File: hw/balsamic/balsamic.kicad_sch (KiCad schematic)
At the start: 50 parts, among them J1 Conn_01x24, J3 USB_B_Mini, SW1 SW_Push, U1 ISP1807-LR-RS, U2 BMI160, U4 MAX77658AANX+

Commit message: switched to mezzanine camera connector
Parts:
- removed AE?: Antenna_Chip, symbol Device:Antenna_Chip
- removed J1: Conn_01x24, Connector_FFC-FPC:Hirose_FH12-24S-0.5SH_1x24-1MP_P0.50mm_Horizontal, symbol Connector_Generic:Conn_01x24
- removed R1, R2, R3: 0, Resistor_SMD:R_0402_1005Metric, symbol Device:R_Small
- removed R17, R18: 0, Resistor_SMD:R_0201_0603Metric, symbol Device:R_Small
- added J2: AXT524124, footprints:PANASONIC_AXT524124, symbol AXT524124-mezzanine-conn:AXT524124
- J3: footprint Connector_USB:USB_Micro-B_Amphenol_10118194_Horizontal -> Connector_USB:USB_Micro-B_GCT_USB3076-30-A
- TP14, TP15, TP16, TP17, TP18, TP19, TP20, TP5: footprint TestPoint:TestPoint_Pad_D1.0mm -> custom_testpoints:TestPoint_Pad_D0.5mm
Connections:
- net +1V8: now also J2.10, J2.11
- net +3V0: now also J2.4
- net +3V3: now also J2.24
- net DVP_D0: now also J2.19
- net DVP_D1: now also J2.21
- net DVP_D2: now also J2.22
- net DVP_D3: now also J2.20
- net DVP_D4: now also J2.18
- net DVP_D5: now also J2.16
- net DVP_D6: now also J2.14
- net DVP_D7: now also J2.12
- net DVP_HSYNC: now also J2.9
- net DVP_PCLK: now also J2.17
- net DVP_PWDN: now also J2.8
- net DVP_RST: now also J2.6
- net DVP_SCL: now also J2.5
- net DVP_SDA: now also J2.3
- net DVP_VSYNC: now also J2.7
- net DVP_XCLK: now also J2.13
- net GND: now also U1.20 (OUT_ANT), U1.22 (OUT_MOD), J2.15, J2.23, J2.S1 (SHIELD), J2.S2 (SHIELD), J2.S3 (SHIELD), J2.S4 (SHIELD)
- net GNDA: now also J2.2
- net nRF_SWDCLK: now also J3.2 (D-)
- net nRF_SWDIO: now also J3.3 (D+)
- no-connect marks 51 -> 52
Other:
- note added: "Need to double check this pin assignment for new connector."
- moved on the sheet: C47, C48, C49, C50, R15, R16

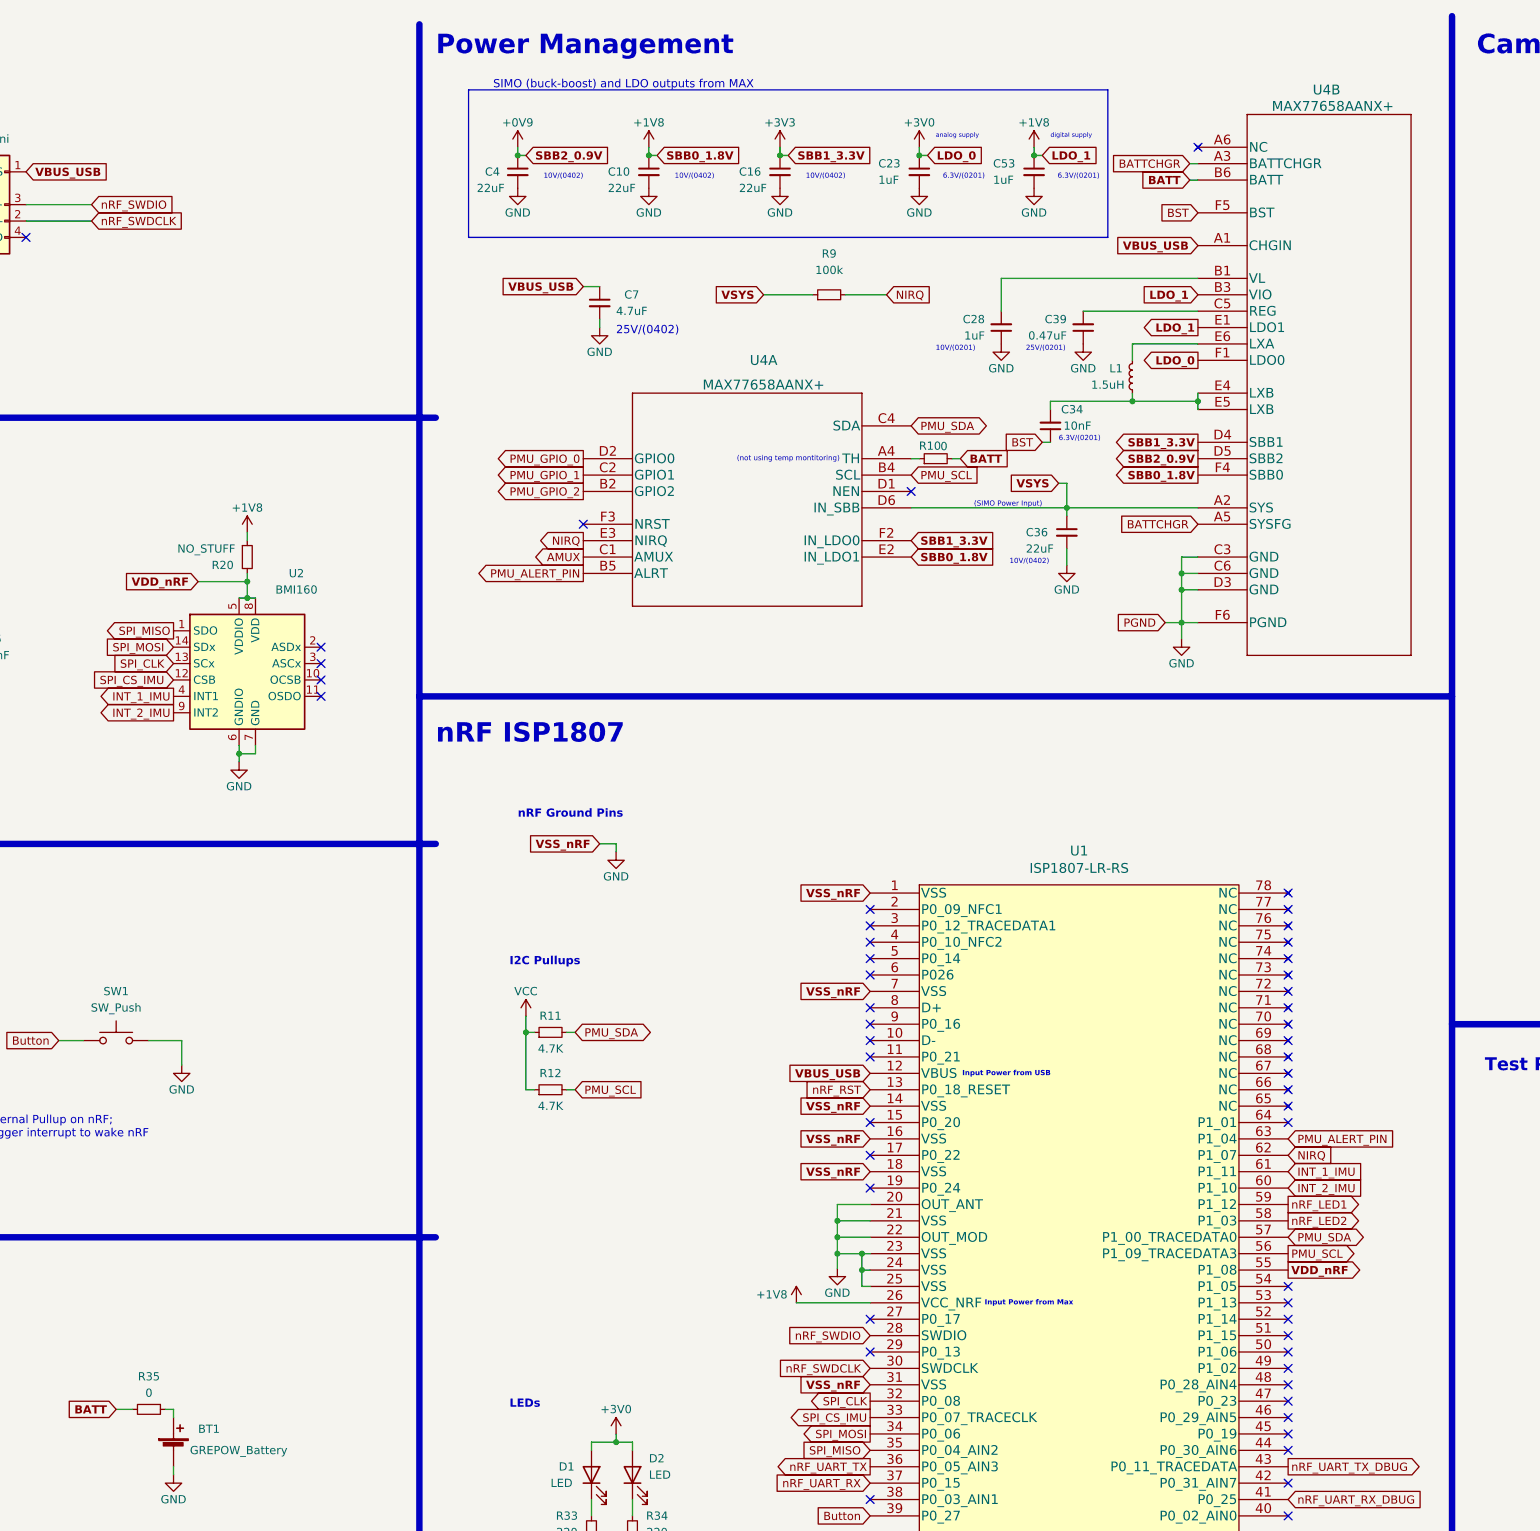
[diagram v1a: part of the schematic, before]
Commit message: changed PMU to MAX77651
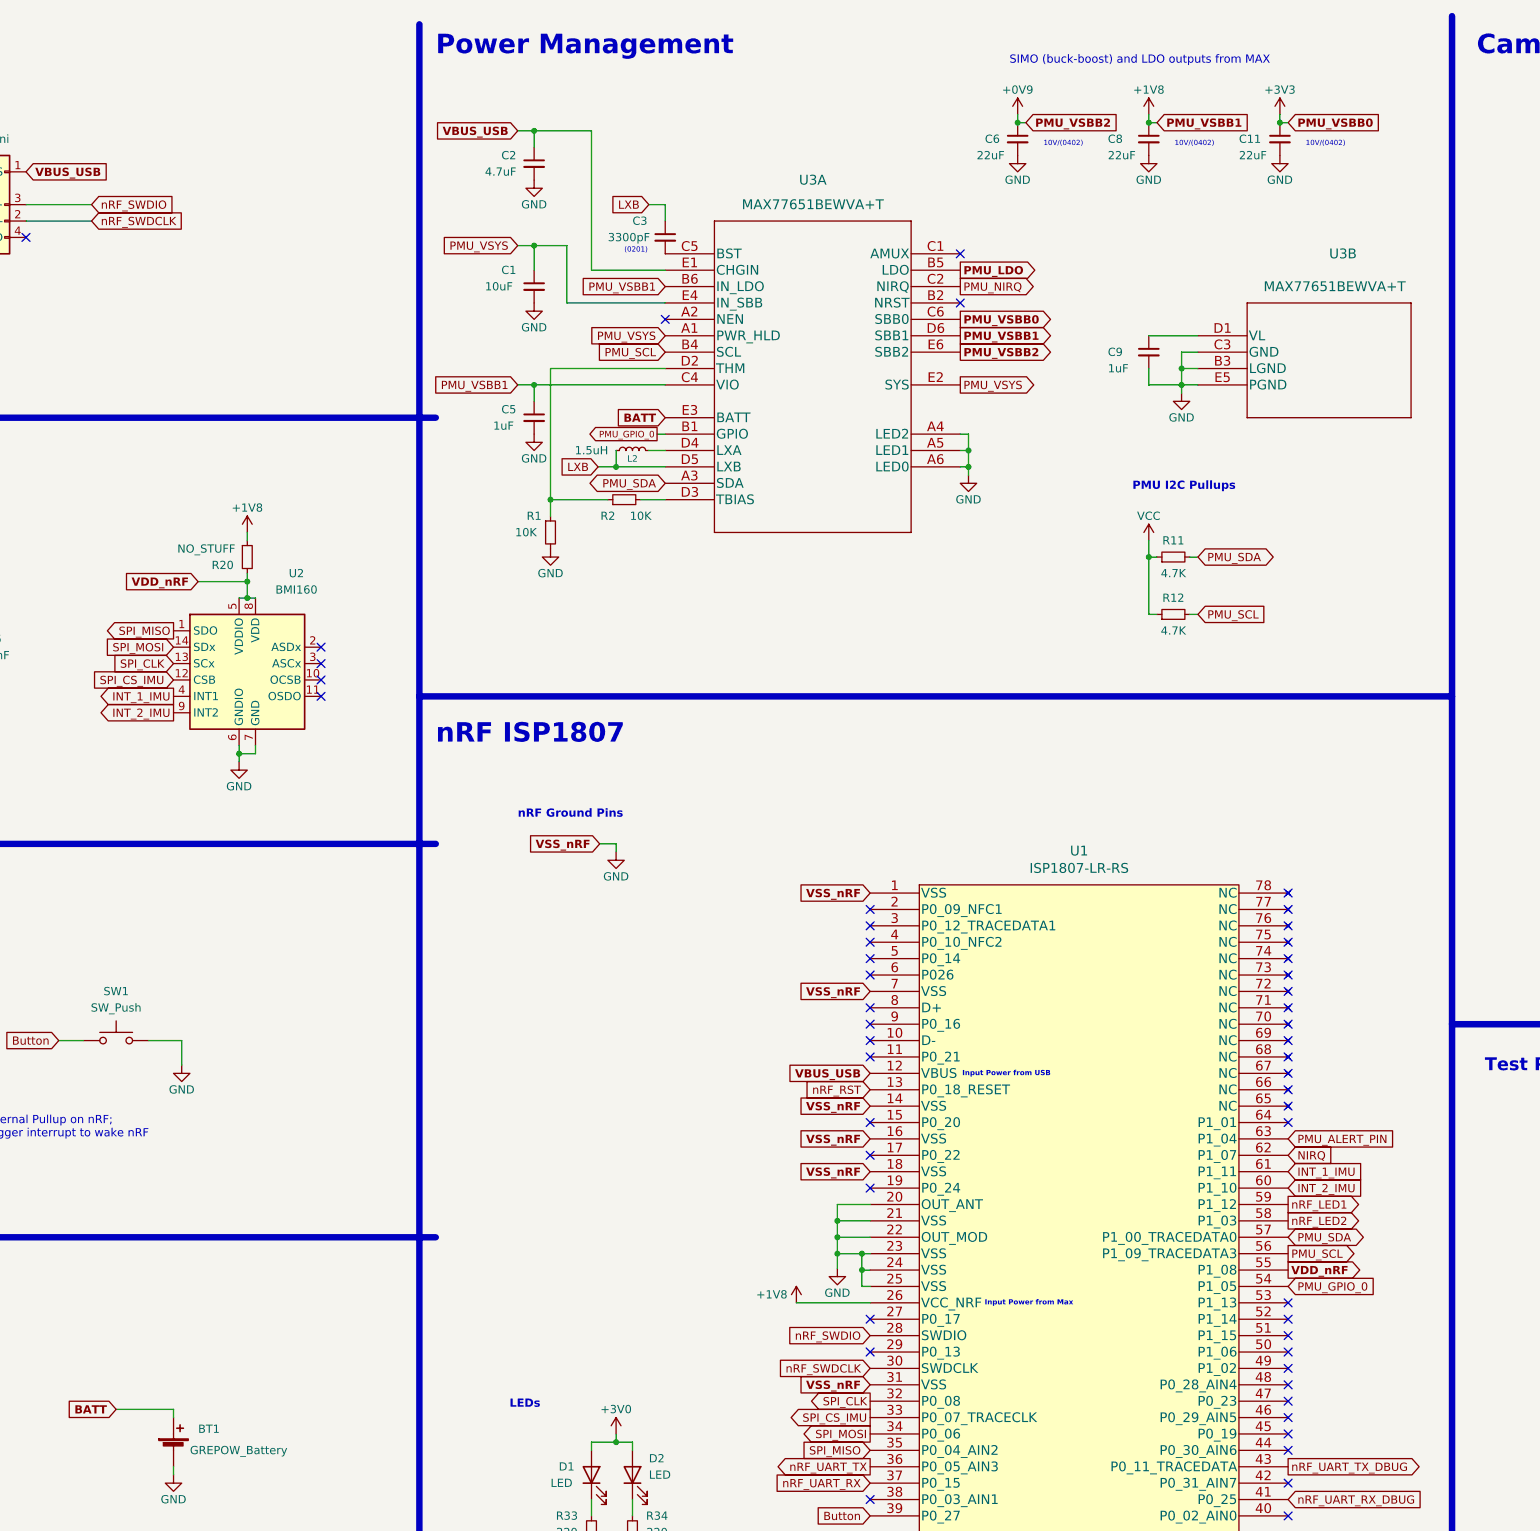
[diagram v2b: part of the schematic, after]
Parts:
- removed C10, C16, C36, C4: 22uF, Capacitor_SMD:C_0201_0603Metric, symbol Device:C_Small
- removed C23, C28, C53: 1uF, Capacitor_SMD:C_0201_0603Metric, symbol Device:C_Small
- removed C34: 10nF, Capacitor_SMD:C_0201_0603Metric, symbol Device:C_Small
- removed C39: 0.47uF, Capacitor_SMD:C_0201_0603Metric, symbol Device:C_Small
- removed C7: 4.7uF, Capacitor_SMD:C_0201_0603Metric, symbol Device:C_Small
- removed L1: 1.5uH, Inductor_SMD:L_0805_2012Metric, symbol Device:L_Small
- removed R10: 0, Resistor_SMD:R_0201_0603Metric, symbol Device:R_Small
- removed R35: 0, Resistor_SMD:R_0402_1005Metric, symbol Device:R_Small
- removed R9: 100k, Resistor_SMD:R_0201_0603Metric, symbol Device:R_Small
- removed U4: MAX77658AANX+, footprints:MAX77658AANX&plus_, symbol max77658_functional:MAX77658AANX+
- added C1: 10uF, Capacitor_SMD:C_0201_0603Metric, symbol Device:C_Small
- added C11, C6, C8: 22uF, Capacitor_SMD:C_0201_0603Metric, symbol Device:C_Small
- added C2: 4.7uF, Capacitor_SMD:C_0201_0603Metric, symbol Device:C_Small
- added C3: 3300pF, Capacitor_SMD:C_0201_0603Metric, symbol Device:C_Small
- added C5, C9: 1uF, Capacitor_SMD:C_0201_0603Metric, symbol Device:C_Small
- added L2: 1.5uH, Inductor_SMD:L_0805_2012Metric, symbol Device:L_Small
- added R1, R2: 10K, Resistor_SMD:R_0201_0603Metric, symbol Device:R_Small
- added U3: MAX77651BEWVA+T, footprints:MAX77651BEWVA&plus_T, symbol MAX77651BEWVA-T:MAX77651BEWVA+T
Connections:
- net +0V9: now also C6.1, U3.E6 (SBB2)
- net +1V8: now also C5.1, C8.1, U3.B6 (IN_LDO), U3.C4 (VIO), U3.D6 (SBB1)
- net +3V3: now also C11.1, U3.C6 (SBB0)
- net BATT: now also BT1.1 (+), U3.E3 (BATT)
- net GND: now also C1.2, C11.2, C2.2, C5.2, C6.2, C8.2, C9.2, R1.2, U3.A4 (LED2), U3.A5 (LED1), U3.A6 (LED0), U3.B3 (LGND), U3.C3 (GND), U3.E5 (PGND)
- net PMU_GPIO_0: now also U1.54 (P1_05), U3.B1 (GPIO)
- net PMU_SCL: now also U3.B4 (SCL)
- net PMU_SDA: now also U3.A3 (SDA)
- net VBUS_USB: now also C2.1, U3.E1 (CHGIN)
- new net: R1.1, R2.1, U3.D2 (THM)
- new net: R2.2, U3.D3 (TBIAS)
- new net: L2.2, U3.D4 (LXA)
- new net: C9.1, U3.D1 (VL)
- new net: C3.2, U3.C5 (BST)
- new net LXB: C3.1, L2.1, U3.D5 (LXB)
- new net PMU_LDO: U3.B5 (LDO)
- new net PMU_NIRQ: U3.C2 (NIRQ)
- new net PMU_VSYS: C1.1, U3.A1 (PWR_HLD), U3.E2 (SYS), U3.E4 (IN_SBB)
- no-connect marks 52 -> 51
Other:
- note added: "(0201)"
- note added: "PMU I2C Pullups"
- note removed: "(SIMO Power Input)"
- note removed: "(not using temp montitoring)"
- note removed: "10V/(0201)"
- note removed: "25V/(0201)"
- note removed: "25V/(0402)"
- note removed: "6.3V/(0201)"
- note removed: "I2C Pullups"
- note removed: "analog supply"
- note removed: "digital supply"
- moved on the sheet: R11, R12

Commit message: Got board size to 16.1x9.825mm
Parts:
- removed C46: 100nF, Capacitor_SMD:C_0402_1005Metric, symbol Device:C_Small
- removed J2: AXT524124, footprints:PANASONIC_AXT524124, symbol AXT524124-mezzanine-conn:AXT524124
- removed R11, R12: 4.7K, Resistor_SMD:R_0201_0603Metric, symbol Device:R_Small
- added C10: 10uF, Capacitor_SMD:C_0201_0603Metric, symbol Device:C_Small
- added C12: 100nf, Capacitor_SMD:C_0201_0603Metric, symbol Device:C_Small
- added C4: 4.7uF, Capacitor_SMD:C_0201_0603Metric, symbol Device:C_Small
- added C7: 22uF, Capacitor_SMD:C_0201_0603Metric, symbol Device:C_Small
- added J1: AXT524124, footprints:PANASONIC_AXT524124, symbol AXT524124-mezzanine-conn:AXT524124
- added TP1, TP10, TP11, TP12, TP13, TP2, TP3, TP4, TP6, TP7, TP8, TP9: TestPoint, custom_testpoints:TestPoint_Pad_D0.5mm, symbol Connector:TestPoint
- C1: value 10uF -> 22uF
- C11, C47, C6, C8: value 22uF -> 10uF
- C48: value 10uF -> 100nF
- L2: footprint Inductor_SMD:L_0805_2012Metric -> Inductor_SMD:L_0603_1608Metric
- R33, R34: value 220 -> 200
- SW1: footprint Button_Switch_SMD:SW_SPST_B3U-1000P -> Resistor_SMD:R_0603_1608Metric
- TP17, TP18, TP19, TP20: footprint custom_testpoints:TestPoint_Pad_D0.5mm -> custom_testpoints:TestPoint_THTPad_1.0x1.0mm_Drill0.5mm
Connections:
- net PMU_LDO is gone; now on net VDDA: U3.B5 (LDO)
- net PMU_SCL is gone; now on net DVP_SCL: U1.56 (P1_09_TRACEDATA3), U3.B4 (SCL)
- net +1V8: now also C6.1, D1.2 (A), D2.2 (A), SW1.2, TP17.1, C12.2, J1.3; no longer C49.1, C50.2
- net BATT: now also C4.1
- net Button: now also TP18.1, U1.33 (P0_07_TRACECLK); no longer U1.39 (P0_27)
- net DVP_D0: now also U1.15 (P0_20), J1.10, TP8.1
- net DVP_D1: now also TP16.1, U1.11 (P0_21), J1.12
- net DVP_D2: now also TP15.1, U1.17 (P0_22), J1.14
- net DVP_D3: now also U1.47 (P0_23), J1.16, TP2.1
- net DVP_D4: now also J1.18
- net DVP_D5: now also J1.20
- net DVP_D6: now also J1.22
- net DVP_D7: now also J1.24
- net DVP_PCLK: now also U1.45 (P0_19), J1.8, TP9.1
- net DVP_SCL: now also J1.11
- net DVP_SDA: now also U1.3 (P0_12_TRACEDATA1), J1.9
- net GND: now also C10.2, C12.1, C4.2, C7.2, J1.19, J1.2, J1.5, J1.6, J1.S1 (SHIELD), J1.S2 (SHIELD), J1.S3 (SHIELD), J1.S4 (SHIELD); no longer SW1.2
- net GNDA: now also J1.23
- net PMU_NIRQ: now also U1.62 (P1_07)
- net PMU_VSYS: now also C7.1
- net nRF_LED1: now also TP19.1, U1.32 (P0_08); no longer U1.59 (P1_12)
- net nRF_LED2: now also TP20.1, U1.34 (P0_06); no longer U1.58 (P1_03)
- net nRF_UART_TX: now also TP7.1
- net IMU_MISO: now reaches U1.19 (P0_24)
- net IMU_MISO: now also U2.1 (SDO), TP3.1
- net DVP_INT: now reaches U1.2 (P0_09_NFC1)
- net DVP_INT: now also J1.7, TP11.1
- net IMU_CLK: now reaches U1.27 (P0_17)
- net IMU_CLK: now also TP5.1, U2.13 (SCx)
- net IMU_CS: now reaches U1.29 (P0_13)
- net IMU_CS: now also U2.12 (CSB), TP6.1
- net nRF_P0_03: now reaches U1.38 (P0_03_AIN1)
- net nRF_P0_02: now reaches U1.40 (P0_02_AIN0)
- net nRF_P0_31: now reaches U1.42 (P0_31_AIN7)
- net nRF_P0_30: now reaches U1.44 (P0_30_AIN6)
- net DVP_FVLD: now reaches U1.46 (P0_29_AIN5)
- net DVP_FVLD: now also J1.15, TP13.1
- net DVP_LVLD: now reaches U1.48 (P0_28_AIN4)
- net DVP_LVLD: now also J1.13, TP12.1
- net IMU_INT2: now reaches U1.49 (P1_02)
- net IMU_INT2: now also U2.9 (INT2)
- net nRF_P1_06: now reaches U1.50 (P1_06)
- net nRF_P1_06: now also C45.2, R20.2, U2.5 (VDDIO), U2.8 (VDD)
- net IMU_INT1: now reaches U1.51 (P1_15)
- net IMU_INT1: now also U2.4 (INT1), TP1.1
- net nRF_P1_14: now reaches U1.52 (P1_14)
- net nRF_P1_13: now reaches U1.53 (P1_13)
- net nRF_P1_01: now reaches U1.64 (P1_01)
- net +0V9 renamed PMU_VSBB2
- net PMU_VSBB2: no longer C6.1
- net +3V0 renamed VDDA
- net VDDA: now also C10.1, J1.21; no longer D1.2 (A), D2.2 (A)
- net +3V3 renamed VDD
- net VDD: now also C49.1, C50.2, J1.1
- removed net INT_1_IMU: TP15.1, U1.61 (P1_11), U2.4 (INT1)
- removed net INT_2_IMU: TP14.1, U1.60 (P1_10), U2.9 (INT2)
- removed net NIRQ: TP5.1, U1.62 (P1_07)
- net PMU_ALERT_PIN renamed nRF_P1_04
- net nRF_P1_04: no longer TP16.1
- removed net SPI_CLK: TP19.1, U1.32 (P0_08), U2.13 (SCx)
- removed net SPI_CS_IMU: TP20.1, U1.33 (P0_07_TRACECLK), U2.12 (CSB)
- removed net SPI_MISO: TP17.1, U1.35 (P0_04_AIN2), U2.1 (SDO)
- removed net SPI_MOSI: TP18.1, U1.34 (P0_06), U2.14 (SDx)
- removed net VDD_nRF: C45.2, R20.2, U1.55 (P1_08), U2.5 (VDDIO), U2.8 (VDD)
- net nRF_RST: no longer names the net of U1.13 (P0_18_RESET)
- net nRF_UART_RX: no longer names the net of U1.37 (P0_15)
- net nRF_UART_RX_DBUG renamed DVP_TRIG
- net DVP_TRIG: now also TP14.1, J1.17
- net nRF_UART_TX_DBUG: no longer names the net of U1.43 (P0_11_TRACEDATA)
- new net DVP_MCLK: J1.4, TP10.1, U1.55 (P1_08)
- new net IMU_MOSI: TP4.1, U1.58 (P1_03), U2.14 (SDx)
- new net nRF_P0_05: U1.35 (P0_04_AIN2)
- new net nRF_P1_10: U1.60 (P1_10)
- new net nRF_P1_11: U1.61 (P1_11)
- new net nRF_P1_12: U1.59 (P1_12)
- no-connect marks 51 -> 32
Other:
- note added: "0603 size pads for button"
- note added: "1.5V"
- note added: "2.8V"
- note added: "BMI270"
- note added: "Connections to 2nd Board"
- note added: "Copied pin assignment used in lattice UPduino shield (see schematic in references folder)"
- note added: "I2C Pullups"
- note added: "May need separate analog and ground planes"
- note added: "QSPI"
- note added: "To Nordic"
- note removed: "Need to double check this pin assignment for new connector."
- note removed: "PMU I2C Pullups"
- note removed: "Will need separate analog and ground planes"
- note removed: "nRF Ground Pins"
- moved on the sheet: BT1, C1, C11, C2, C3, C45, C47, C48, C49, C5, C50, C8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
